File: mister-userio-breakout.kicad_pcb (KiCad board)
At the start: 2 copper layers, 28.5 x 19.8 mm, 2 parts

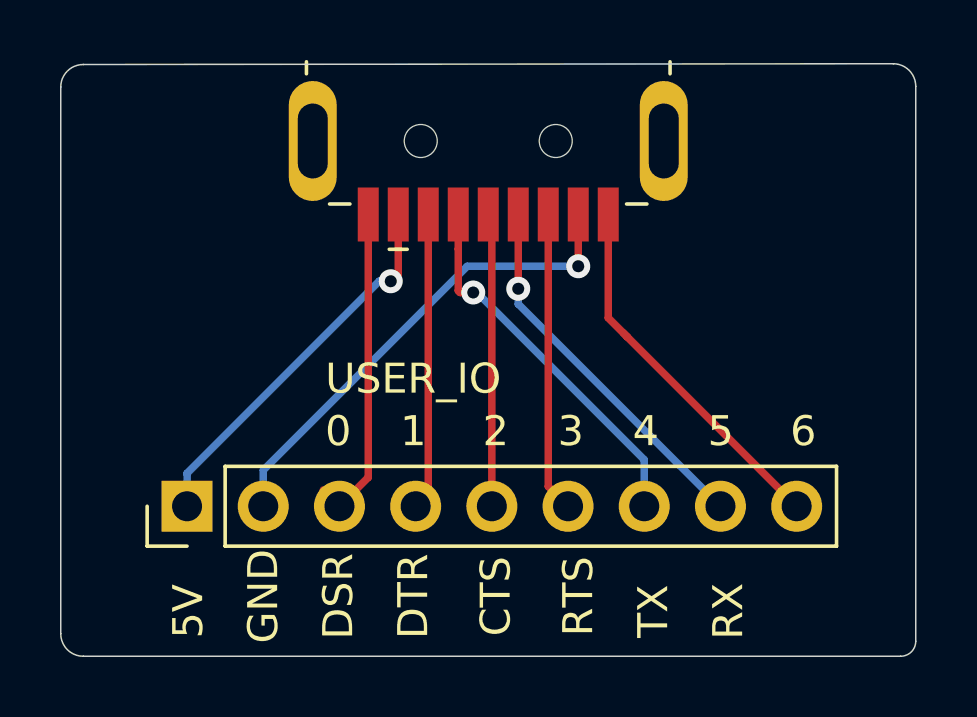
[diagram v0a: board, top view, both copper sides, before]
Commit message: add USB signal names to the bottom
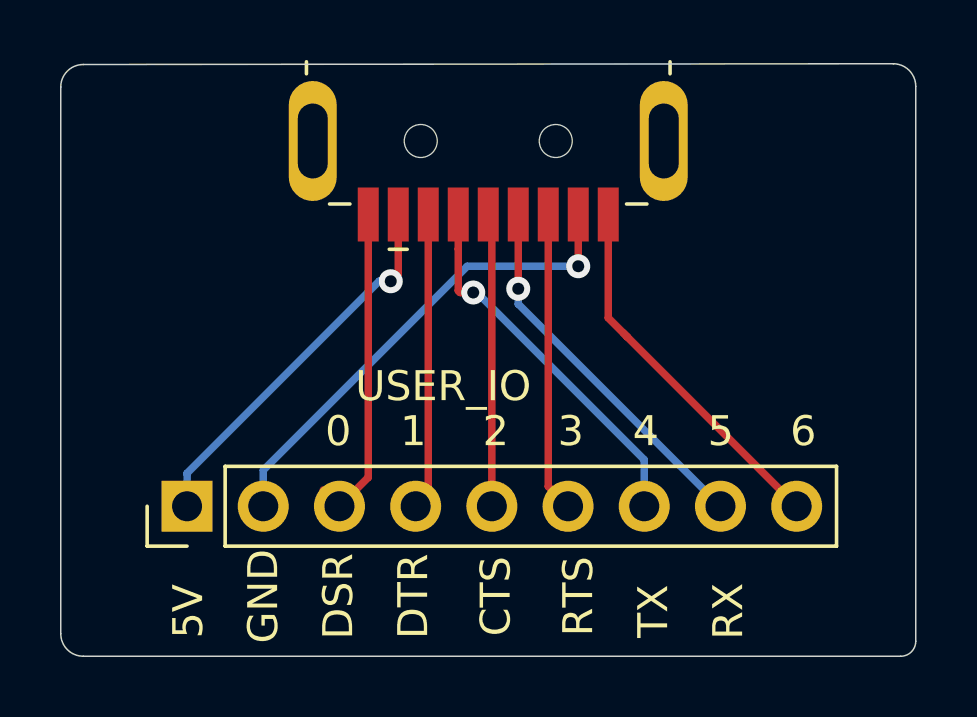
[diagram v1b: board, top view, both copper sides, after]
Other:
- board text added: "D+"
- board text added: "D-"
- board text added: "DRAIN"
- board text added: "SSRX+"
- board text added: "SSRX-"
- board text added: "SSTX+"
- board text added: "SSTX-"
- board text added: "VBUS"
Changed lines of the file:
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@@
   (general
     (thickness 1.6)
-    (drawings 24)
+    (drawings 33)
     (tracks 43)
     (zones 0)
@@
     )
   )
-  (gr_text USER_IO (at 95 66.75) (layer F.SilkS)
+  (gr_text DRAIN (at 97.75 67 90) (layer B.SilkS)
+    (effects (font (size 1 1) (thickness 0.15)) (justify mirror))
+  )
+  (gr_text GND (at 90.25 67.5 90) (layer B.SilkS)
+    (effects (font (size 1 1) (thickness 0.15)) (justify mirror))
+  )
+  (gr_text SSTX+ (at 93 66.75 90) (layer B.SilkS)
+    (effects (font (size 1 1) (thickness 0.15)) (justify mirror))
+  )
+  (gr_text SSTX- (at 95.25 66.5 90) (layer B.SilkS)
+    (effects (font (size 1 1) (thickness 0.15)) (justify mirror))
+  )
+  (gr_text SSRX+ (at 100.25 66.5 90) (layer B.SilkS)
+    (effects (font (size 1 1) (thickness 0.15)) (justify mirror))
+  )
+  (gr_text SSRX- (at 108 66.5 90) (layer B.SilkS)
+    (effects (font (size 1 1) (thickness 0.15)) (justify mirror))
+  )
+  (gr_text D- (at 102.75 68 90) (layer B.SilkS)
+    (effects (font (size 1 1) (thickness 0.15)) (justify mirror))
+  )
+  (gr_text D+ (at 105.25 68 90) (layer B.SilkS)
+    (effects (font (size 1 1) (thickness 0.15)) (justify mirror))
+  )
+  (gr_text VBUS (at 87.75 67 90) (layer B.SilkS)
+    (effects (font (size 1 1) (thickness 0.15)) (justify mirror))
+  )
+  (gr_text USER_IO (at 96 67) (layer F.SilkS)
     (effects (font (size 1 1) (thickness 0.15)))
   )

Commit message: more silkscreen tweaks and bring in the board edge
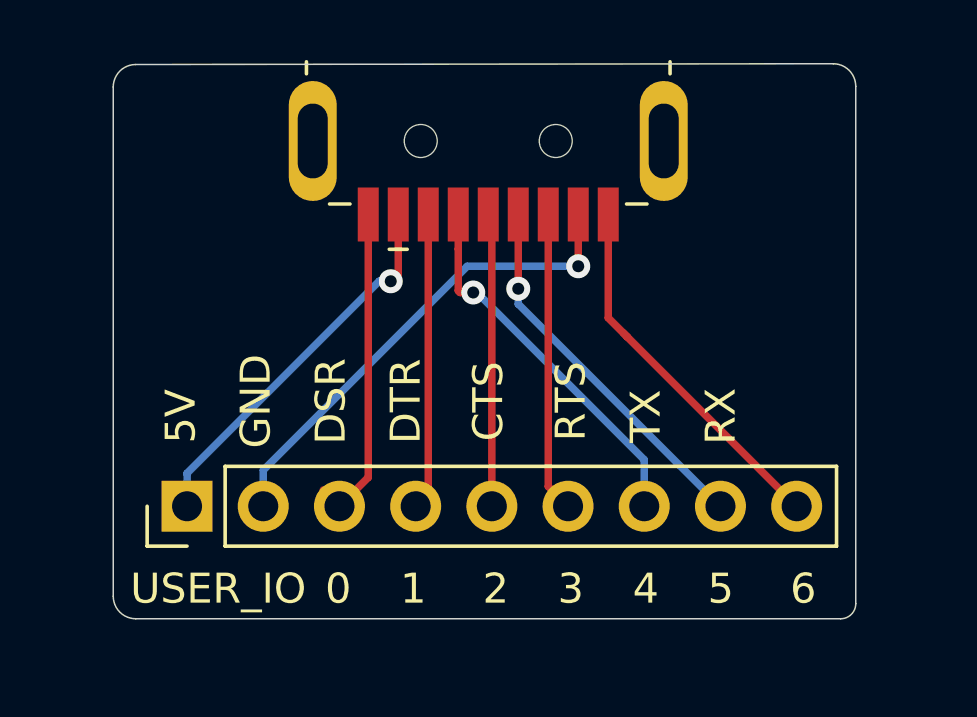
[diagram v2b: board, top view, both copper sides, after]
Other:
- board size 28.5 x 19.8 mm -> 24.8 x 18.5 mm
- board text added: "7"
- board text added: "8"
- board text added: "9"
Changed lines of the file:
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@@
   (general
     (thickness 1.6)
-    (drawings 33)
+    (drawings 42)
     (tracks 43)
     (zones 0)
@@
     )
   )
+  (gr_text 5 (at 108 73.5) (layer B.SilkS)
+    (effects (font (size 1 1) (thickness 0.15)) (justify mirror))
+  )
+  (gr_text 3 (at 105.25 73.5) (layer B.SilkS)
+    (effects (font (size 1 1) (thickness 0.15)) (justify mirror))
+  )
+  (gr_text 2 (at 102.75 73.5) (layer B.SilkS)
+    (effects (font (size 1 1) (thickness 0.15)) (justify mirror))
+  )
+  (gr_text 6 (at 100.25 73.5) (layer B.SilkS)
+    (effects (font (size 1 1) (thickness 0.15)) (justify mirror))
+  )
+  (gr_text 7 (at 97.75 73.5) (layer B.SilkS)
+    (effects (font (size 1 1) (thickness 0.15)) (justify mirror))
+  )
+  (gr_text 8 (at 95 73.5) (layer B.SilkS)
+    (effects (font (size 1 1) (thickness 0.15)) (justify mirror))
+  )
+  (gr_text 9 (at 92.5 73.5) (layer B.SilkS)
+    (effects (font (size 1 1) (thickness 0.15)) (justify mirror))
+  )
+  (gr_text 4 (at 90 73.5) (layer B.SilkS)
+    (effects (font (size 1 1) (thickness 0.15)) (justify mirror))
+  )
+  (gr_text 1 (at 87.5 73.5) (layer B.SilkS)
+    (effects (font (size 1 1) (thickness 0.15)) (justify mirror))
+  )
   (gr_text DRAIN (at 97.75 67 90) (layer B.SilkS)
     (effects (font (size 1 1) (thickness 0.15)) (justify mirror))
@@
     (effects (font (size 1 1) (thickness 0.15)) (justify mirror))
   )
-  (gr_text USER_IO (at 96 67) (layer F.SilkS)
-    (effects (font (size 1 1) (thickness 0.15)))
-  )
-  (gr_arc (start 84 57.025) (end 84 56.275) (angle -90) (layer Edge.Cuts) (width 0.05))
-  (gr_arc (start 111.25 75.5) (end 111.25 76) (angle -90) (layer Edge.Cuts) (width 0.05))
-  (gr_text RX (at 105.5 74.5 90) (layer F.SilkS)
-    (effects (font (size 1 1) (thickness 0.15)))
-  )
-  (gr_text TX (at 103 74.5 90) (layer F.SilkS)
-    (effects (font (size 1 1) (thickness 0.15)))
-  )
-  (gr_text RTS (at 100.5 74 90) (layer F.SilkS)
-    (effects (font (size 1 1) (thickness 0.15)))
-  )
-  (gr_text CTS (at 97.75 74 90) (layer F.SilkS)
-    (effects (font (size 1 1) (thickness 0.15)))
-  )
-  (gr_text DTR (at 95 74 90) (layer F.SilkS)
-    (effects (font (size 1 1) (thickness 0.15)))
-  )
-  (gr_text DSR (at 92.5 74 90) (layer F.SilkS)
-    (effects (font (size 1 1) (thickness 0.15)))
-  )
-  (gr_text 6 (at 108 68.5) (layer F.SilkS)
-    (effects (font (size 1 1) (thickness 0.15)))
-  )
-  (gr_text 5 (at 105.25 68.5) (layer F.SilkS)
-    (effects (font (size 1 1) (thickness 0.15)))
-  )
-  (gr_text 4 (at 102.75 68.5) (layer F.SilkS)
-    (effects (font (size 1 1) (thickness 0.15)))
-  )
-  (gr_text 3 (at 100.25 68.5) (layer F.SilkS)
-    (effects (font (size 1 1) (thickness 0.15)))
-  )
-  (gr_text GND (at 90 74 90) (layer F.SilkS)
-    (effects (font (size 1 1) (thickness 0.15)))
-  )
-  (gr_text 2 (at 97.75 68.5) (layer F.SilkS)
-    (effects (font (size 1 1) (thickness 0.15)))
-  )
-  (gr_text 0 (at 92.5 68.5) (layer F.SilkS)
-    (effects (font (size 1 1) (thickness 0.15)))
-  )
-  (gr_text 1 (at 95 68.5) (layer F.SilkS)
-    (effects (font (size 1 1) (thickness 0.15)))
-  )
-  (gr_text 5V (at 87.5 74.5 90) (layer F.SilkS)
-    (effects (font (size 1 1) (thickness 0.15)))
-  )
-  (gr_line (start 83.25 57.025) (end 83.25 75.25) (layer Edge.Cuts) (width 0.05))
-  (gr_arc (start 84 75.25) (end 83.25 75.25) (angle -90) (layer Edge.Cuts) (width 0.05))
-  (gr_line (start 84 56.275) (end 111 56.25) (layer Edge.Cuts) (width 0.05))
-  (gr_line (start 111.75 75.5) (end 111.75 57) (layer Edge.Cuts) (width 0.05))
-  (gr_line (start 84 76) (end 111.25 76) (layer Edge.Cuts) (width 0.05))
-  (gr_arc (start 111 57) (end 111.75 57) (angle -90) (layer Edge.Cuts) (width 0.05))
+  (gr_text USER_IO (at 88.5 73.75) (layer F.SilkS)
+    (effects (font (size 1 1) (thickness 0.15)))
+  )
+  (gr_arc (start 85.75 57.025) (end 85.75 56.275) (angle -90) (layer Edge.Cuts) (width 0.05))
+  (gr_arc (start 109.25 74.25) (end 109.25 74.75) (angle -90) (layer Edge.Cuts) (width 0.05))
+  (gr_text RX (at 105.25 68 90) (layer F.SilkS)
+    (effects (font (size 1 1) (thickness 0.15)))
+  )
+  (gr_text TX (at 102.75 68 90) (layer F.SilkS)
+    (effects (font (size 1 1) (thickness 0.15)))
+  )
+  (gr_text RTS (at 100.25 67.5 90) (layer F.SilkS)
+    (effects (font (size 1 1) (thickness 0.15)))
+  )
+  (gr_text CTS (at 97.5 67.5 90) (layer F.SilkS)
+    (effects (font (size 1 1) (thickness 0.15)))
+  )
+  (gr_text DTR (at 94.75 67.5 90) (layer F.SilkS)
+    (effects (font (size 1 1) (thickness 0.15)))
+  )
+  (gr_text DSR (at 92.25 67.5 90) (layer F.SilkS)
+    (effects (font (size 1 1) (thickness 0.15)))
+  )
+  (gr_text 6 (at 108 73.75) (layer F.SilkS)
+    (effects (font (size 1 1) (thickness 0.15)))
+  )
+  (gr_text 5 (at 105.25 73.75) (layer F.SilkS)
+    (effects (font (size 1 1) (thickness 0.15)))
+  )
+  (gr_text 4 (at 102.75 73.75) (layer F.SilkS)
+    (effects (font (size 1 1) (thickness 0.15)))
+  )
+  (gr_text 3 (at 100.25 73.75) (layer F.SilkS)
+    (effects (font (size 1 1) (thickness 0.15)))
+  )
+  (gr_text GND (at 89.75 67.5 90) (layer F.SilkS)
+    (effects (font (size 1 1) (thickness 0.15)))
+  )
+  (gr_text 2 (at 97.75 73.75) (layer F.SilkS)
+    (effects (font (size 1 1) (thickness 0.15)))
+  )
+  (gr_text 0 (at 92.5 73.75) (layer F.SilkS)
+    (effects (font (size 1 1) (thickness 0.15)))
+  )
+  (gr_text 1 (at 95 73.75) (layer F.SilkS)
+    (effects (font (size 1 1) (thickness 0.15)))
+  )
+  (gr_text 5V (at 87.25 68 90) (layer F.SilkS)
+    (effects (font (size 1 1) (thickness 0.15)))
+  )
+  (gr_line (start 85 57.025) (end 85 74) (layer Edge.Cuts) (width 0.05))
+  (gr_arc (start 85.75 74) (end 85 74) (angle -90) (layer Edge.Cuts) (width 0.05))
+  (gr_line (start 85.75 56.275) (end 109 56.25) (layer Edge.Cuts) (width 0.05))
+  (gr_line (start 109.75 74.25) (end 109.75 57) (layer Edge.Cuts) (width 0.05))
+  (gr_line (start 85.75 74.75) (end 109.25 74.75) (layer Edge.Cuts) (width 0.05))
+  (gr_arc (start 109 57) (end 109.75 57) (angle -90) (layer Edge.Cuts) (width 0.05))
   (segment (start 87 70.54) (end 87.46 71) (width 0.25) (layer F.Cu) (net 0))
   (segment (start 108 70.78) (end 107.78 71) (width 0.25) (layer F.Cu) (net 0))

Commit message: corrections!
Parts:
- moved REF** 0.50 mm to (87.0, 71.0)
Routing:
- net (no net): track 110.0 -> 131.1 mm, vias 4 -> 5
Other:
- board text removed: "7"
- board text removed: "8"
- board text removed: "9"
